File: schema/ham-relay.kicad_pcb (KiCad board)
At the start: 2 copper layers, 140 x 98 mm, 66 parts, among them J1 DB9, P1 JTAG, P2 CONN_01X08, P3 RESET, P4 ISP, P5 CONN_01X03, U1 REG3V3, U2 LPC1114FN28/102, U3 CPC1017N, U4 XYZ, U5 XYZ, U6 TBB1458, U7 74HC126N

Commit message: Design rules
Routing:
- net VCC: track 129.4 -> 0.00 mm
- net /SWDIO: track 48.3 -> 0.00 mm
- net +12V: track 24.8 -> 0.00 mm
- net /RX_CR: track 19.7 -> 0.00 mm
- net /TONE: track 15.5 -> 0.00 mm
- net Net-(P1-Pad17): track 12.1 -> 0.00 mm
- net Net-(P1-Pad11): track 10.8 -> 0.00 mm
- net /TONE_SW: track 8.26 -> 0.00 mm
- net Net-(D1-Pad2): track 7.03 -> 0.00 mm
- net VCC/2: track 6.98 -> 0.00 mm
- net Net-(D4-Pad2): track 6.26 -> 0.00 mm
- net Net-(D6-Pad2): track 6.19 -> 0.00 mm
- net Net-(D3-Pad2): track 6.18 -> 0.00 mm
- net Net-(D5-Pad2): track 6.17 -> 0.00 mm
- net Net-(R10-Pad2): track 5.71 -> 0.00 mm
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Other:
- net class Default: clearance 0.5 -> 0.2032; trace_width 1 -> 0.1524; via_dia 2.5 -> 0.65; via_drill 1 -> 0.3
- net class Small removed
- rule trace_clearance: 0.5 -> 0.2032
- rule trace_min: 0.2 -> 0.15
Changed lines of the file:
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@@
   (general
     (links 151)
-    (no_connects 128)
-    (area 57.709999 38.024999 197.860001 136.175001)
+    (no_connects 151)
+    (area -486.6365 -522.26 736.73 673.46449)
     (thickness 1.6)
     (drawings 8)
-    (tracks 54)
+    (tracks 0)
     (zones 0)
     (modules 66)
@@
   )
   (setup
-    (last_trace_width 1)
-    (trace_clearance 0.5)
+    (last_trace_width 0.1524)
+    (trace_clearance 0.2032)
     (zone_clearance 0.254)
     (zone_45_only yes)
-    (trace_min 0.2)
+    (trace_min 0.15)
     (segment_width 0.2)
     (edge_width 0.15)
-    (via_size 2.5)
-    (via_drill 1)
+    (via_size 0.65)
+    (via_drill 0.3)
     (via_min_size 0.4)
     (via_min_drill 0.3)
@@
   (net 49 "Net-(U2-Pad28)")
   (net_class Default "This is the default net class."
-    (clearance 0.5)
-    (trace_width 1)
-    (via_dia 2.5)
-    (via_drill 1)
+    (clearance 0.2032)
+    (trace_width 0.1524)
+    (via_dia 0.65)
+    (via_drill 0.3)
     (uvia_dia 0.3)
     (uvia_drill 0.1)
@@
     (add_net VCC)
     (add_net VCC/2)
-  )
-  (net_class Small ""
-    (clearance 508)
-    (trace_width 254)
-    (via_dia 2.5)
-    (via_drill 1)
-    (uvia_dia 0.3)
-    (uvia_drill 0.1)
   )
   (module Pin_Headers:Pin_Header_Straight_2x10 (layer F.Cu)
@@
   (gr_line (start 57.785 38.1) (end 197.785 38.1) (angle 90) (layer Edge.Cuts) (width 0.15))
   (gr_line (start 57.785 38.1) (end 57.785 136.1) (angle 90) (layer Edge.Cuts) (width 0.15))
-  (segment (start 80.01 76.835) (end 82.55 76.835) (width 1) (layer B.Cu) (net 2))
-  (segment (start 191.135 50.165) (end 189.865 50.165) (width 1) (layer B.Cu) (net 5))
-  (segment (start 193.04 64.77) (end 194.945 62.865) (width 1) (layer B.Cu) (net 5))
-  (segment (start 194.945 62.865) (end 194.945 53.975) (width 1) (layer B.Cu) (net 5))
-  (segment (start 194.945 53.975) (end 191.135 50.165) (width 1) (layer B.Cu) (net 5))
-  (segment (start 193.04 68.505) (end 193.04 64.77) (width 1) (layer B.Cu) (net 5))
-  (segment (start 189.27064 49.57064) (end 189.27064 47.625) (width 1) (layer B.Cu) (net 5))
-  (segment (start 189.865 50.165) (end 189.27064 49.57064) (width 1) (layer B.Cu) (net 5))
-  (segment (start 185.42 64.135) (end 187.96 64.135) (width 1) (layer B.Cu) (net 6))
-  (segment (start 187.96 64.135) (end 191.135 60.96) (width 1) (layer B.Cu) (net 6))
-  (segment (start 193.04 98.505) (end 188.675 98.505) (width 1) (layer B.Cu) (net 8))
-  (segment (start 188.595 104.14) (end 184.15 104.14) (width 1) (layer B.Cu) (net 8))
-  (segment (start 188.595 98.585) (end 188.595 104.14) (width 1) (layer B.Cu) (net 8))
-  (segment (start 188.675 98.505) (end 188.595 98.585) (width 1) (layer B.Cu) (net 8))
-  (segment (start 179.705 106.045) (end 182.245 106.045) (width 1) (layer B.Cu) (net 8))
-  (segment (start 182.245 106.045) (end 184.15 104.14) (width 1) (layer B.Cu) (net 8))
-  (segment (start 71.755 61.595) (end 66.29 61.595) (width 1) (layer B.Cu) (net 10))
-  (segment (start 66.29 61.595) (end 65.785 62.1) (width 1) (layer B.Cu) (net 10))
-  (segment (start 71.755 48.26) (end 65.945 48.26) (width 1) (layer B.Cu) (net 11))
-  (segment (start 65.945 48.26) (end 65.785 48.1) (width 1) (layer B.Cu) (net 11))
-  (segment (start 65.945 48.26) (end 65.785 48.1) (width 1) (layer F.Cu) (net 11))
-  (segment (start 71.755 54.61) (end 66.275 54.61) (width 1) (layer B.Cu) (net 12))
-  (segment (start 66.275 54.61) (end 65.785 55.1) (width 1) (layer B.Cu) (net 12))
-  (segment (start 151.765 95.885) (end 151.765 87.63) (width 1) (layer B.Cu) (net 15))
-  (segment (start 127 91.44) (end 137.16 91.44) (width 1) (layer B.Cu) (net 16))
-  (segment (start 137.16 91.44) (end 140.97 87.63) (width 1) (layer B.Cu) (net 16))
-  (segment (start 168.275 90.805) (end 172.085 90.805) (width 1) (layer B.Cu) (net 18))
-  (segment (start 173.94936 47.625) (end 173.94936 47.58436) (width 1) (layer B.Cu) (net 19))
-  (segment (start 173.94936 47.58436) (end 173.90872 47.625) (width 1) (layer B.Cu) (net 19))
-  (segment (start 173.90872 47.625) (end 80.01 47.625) (width 1) (layer B.Cu) (net 19))
-  (segment (start 80.01 47.625) (end 79.375 48.26) (width 1) (layer B.Cu) (net 19))
-  (segment (start 171.45 56.515) (end 171.45 55.20436) (width 1) (layer B.Cu) (net 19))
-  (segment (start 171.45 55.20436) (end 173.94936 52.705) (width 1) (layer B.Cu) (net 19))
-  (segment (start 179.705 64.135) (end 179.705 62.23) (width 1) (layer B.Cu) (net 19))
-  (segment (start 179.705 62.23) (end 185.42 56.515) (width 1) (layer B.Cu) (net 19))
-  (segment (start 171.45 56.515) (end 165.735 56.515) (width 1) (layer B.Cu) (net 19))
-  (segment (start 171.45 56.515) (end 174.625 56.515) (width 1) (layer B.Cu) (net 19))
-  (segment (start 174.625 56.515) (end 179.07 56.515) (width 1) (layer B.Cu) (net 19))
-  (segment (start 179.07 56.515) (end 185.42 56.515) (width 1) (layer B.Cu) (net 19))
-  (segment (start 161.925 65.405) (end 165.735 65.405) (width 1) (layer B.Cu) (net 20))
-  (segment (start 165.735 67.31) (end 165.735 65.405) (width 1) (layer B.Cu) (net 20))
-  (segment (start 165.735 65.405) (end 165.735 64.135) (width 1) (layer B.Cu) (net 20))
-  (segment (start 71.755 68.58) (end 66.305 68.58) (width 1) (layer B.Cu) (net 23))
-  (segment (start 66.305 68.58) (end 65.785 69.1) (width 1) (layer B.Cu) (net 23))
-  (segment (start 80.01 84.455) (end 75.565 84.455) (width 1) (layer B.Cu) (net 25))
-  (segment (start 99.06 87.63) (end 99.06 91.44) (width 1) (layer B.Cu) (net 25))
-  (segment (start 85.09 73.66) (end 99.06 87.63) (width 1) (layer B.Cu) (net 25))
-  (segment (start 75.565 73.66) (end 85.09 73.66) (width 1) (layer B.Cu) (net 25))
-  (segment (start 75.565 84.455) (end 75.565 73.66) (width 1) (layer B.Cu) (net 25))
-  (segment (start 151.765 80.01) (end 146.05 80.01) (width 1) (layer B.Cu) (net 36))
-  (segment (start 69.215 89.535) (end 80.01 89.535) (width 1) (layer B.Cu) (net 41))
-  (segment (start 69.215 93.98) (end 73.025 93.98) (width 1) (layer B.Cu) (net 42))
-  (segment (start 76.2 97.155) (end 80.01 97.155) (width 1) (layer B.Cu) (net 42))
-  (segment (start 73.025 93.98) (end 76.2 97.155) (width 1) (layer B.Cu) (net 42))
   (zone (net 0) (net_name "") (layer F.Cu) (hatch edge 0.508)
     (connect_pads (clearance 0))

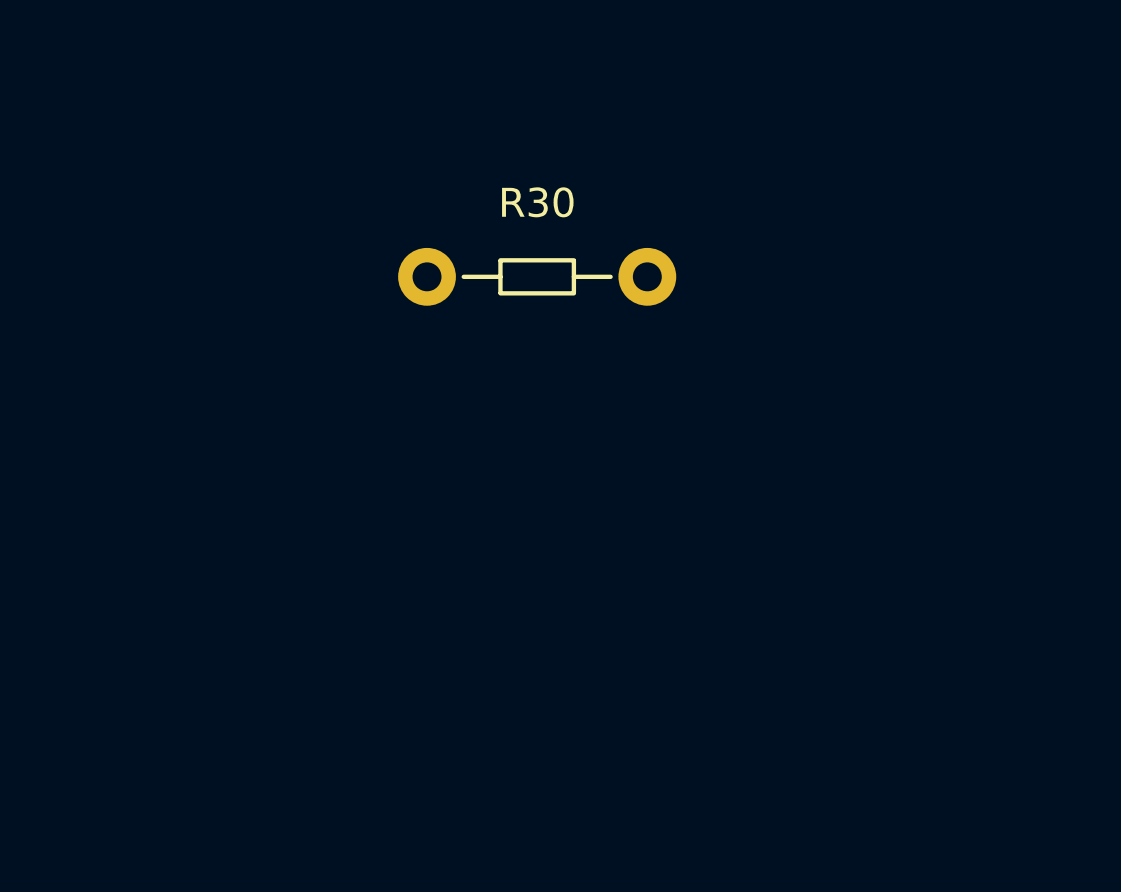
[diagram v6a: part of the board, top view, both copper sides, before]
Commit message: Add EXT_CR support
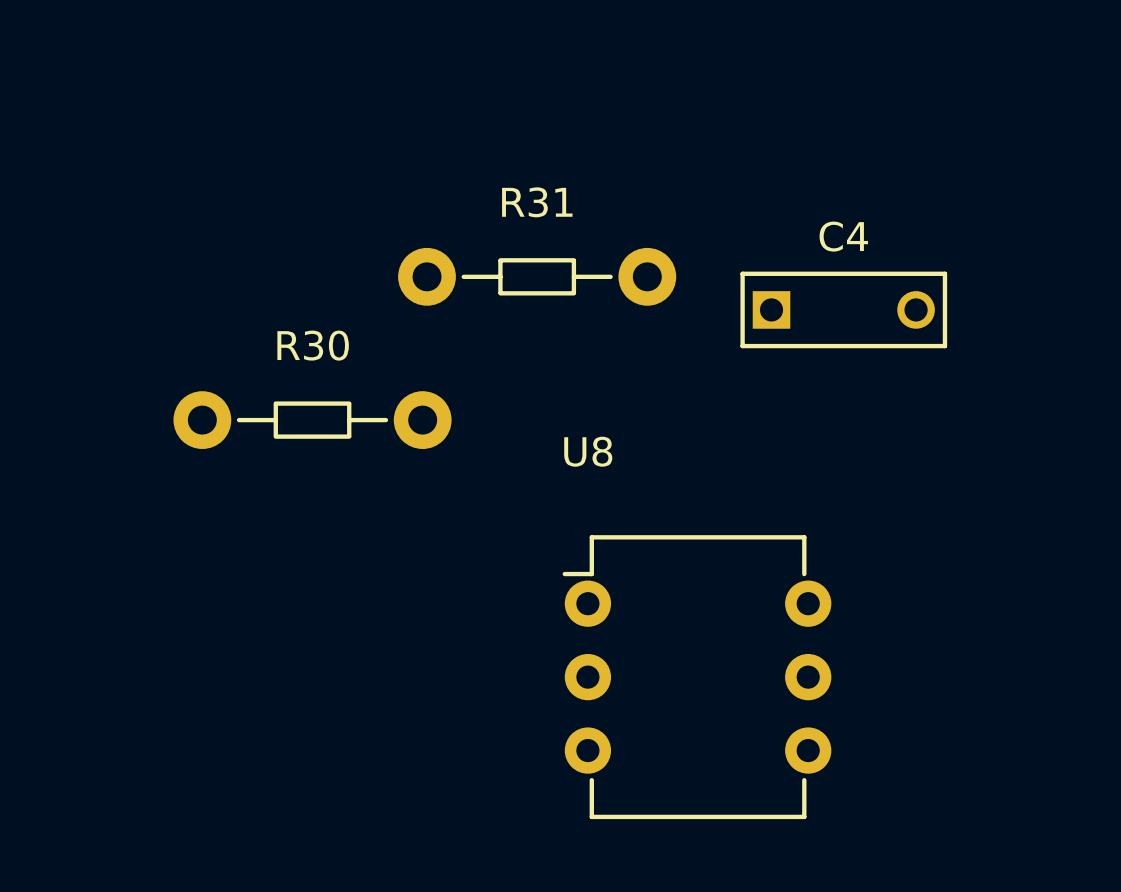
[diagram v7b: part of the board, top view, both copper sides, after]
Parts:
- added C4: 10nF, Capacitors_ThroughHole:C_Rect_L7_W2.5_P5, F.Cu at (135.9, 147.3)
- added R31: ?, resistors:Resistor_Horizontal_RM08mm, F.Cu at (127.8, 146.2)
- added U8: XYZ, Housings_DIP:DIP-6_W7.62mm, F.Cu at (129.5, 157.5)
- moved R30 9.22 mm to (120.0, 151.1)
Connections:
- P2 pad 4: /Audio/AUDIO_IN -> /EXT_CR
- P2 pad 5: /Audio/AUDIO_OUT -> /Audio/AUDIO_IN
- P2 pad 6: (no net) -> /Audio/AUDIO_OUT
- U1 pad 1: VCC -> (no net)
- U1 pad 2: GND -> (no net)
- U1 pad 3: +3V3 -> (no net)
- U2 pad 26: (no net) -> /EXT
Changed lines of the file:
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@@
 (kicad_pcb (version 4) (host pcbnew 4.0.1-stable)
   (general
-    (links 151)
-    (no_connects 151)
-    (area -486.6365 -522.26 736.73 673.46449)
+    (links 155)
+    (no_connects 155)
+    (area 57.709999 38.024999 197.860001 136.175001)
     (thickness 1.6)
     (drawings 8)
     (tracks 0)
     (zones 0)
-    (modules 66)
-    (nets 50)
+    (modules 69)
+    (nets 53)
   )
   (page A4)
@@
   (net 48 "Net-(U2-Pad9)")
   (net 49 "Net-(U2-Pad28)")
+  (net 50 /EXT_CR)
+  (net 51 "Net-(R31-Pad2)")
+  (net 52 /EXT)
   (net_class Default "This is the default net class."
     (clearance 0.2032)
@@
     (add_net /Audio/AUDIO_OUT)
     (add_net /Audio/TONE)
+    (add_net /EXT)
+    (add_net /EXT_CR)
     (add_net /ISP)
     (add_net /RESET)
@@
     (add_net "Net-(R26-Pad2)")
     (add_net "Net-(R30-Pad1)")
+    (add_net "Net-(R31-Pad2)")
     (add_net "Net-(U2-Pad28)")
     (add_net "Net-(U2-Pad5)")
@@
       (net 43 /ISP))
     (pad 25 thru_hole oval (at 15.24 7.62 270) (size 1.6 1.6) (drill 0.8) (layers *.Cu *.Mask F.SilkS))
-    (pad 26 thru_hole oval (at 15.24 5.08 270) (size 1.6 1.6) (drill 0.8) (layers *.Cu *.Mask F.SilkS))
+    (pad 26 thru_hole oval (at 15.24 5.08 270) (size 1.6 1.6) (drill 0.8) (layers *.Cu *.Mask F.SilkS)
+      (net 52 /EXT))
     (pad 27 thru_hole oval (at 15.24 2.54 270) (size 1.6 1.6) (drill 0.8) (layers *.Cu *.Mask F.SilkS)
       (net 14 /RXE))
@@
       (net 5 +12V))
     (pad 7 thru_hole circle (at 30 0 90) (size 2.5 2.5) (drill 1.3) (layers *.Cu *.Mask F.SilkS))
-    (pad 6 thru_hole circle (at 25 0 90) (size 2.5 2.5) (drill 1.3) (layers *.Cu *.Mask F.SilkS))
+    (pad 6 thru_hole circle (at 25 0 90) (size 2.5 2.5) (drill 1.3) (layers *.Cu *.Mask F.SilkS)
+      (net 24 /Audio/AUDIO_OUT))
     (pad 5 thru_hole circle (at 20 0 90) (size 2.5 2.5) (drill 1.3) (layers *.Cu *.Mask F.SilkS)
-      (net 24 /Audio/AUDIO_OUT))
+      (net 28 /Audio/AUDIO_IN))
     (pad 4 thru_hole circle (at 15 0 90) (size 2.5 2.5) (drill 1.3) (layers *.Cu *.Mask F.SilkS)
-      (net 28 /Audio/AUDIO_IN))
+      (net 50 /EXT_CR))
     (pad 3 thru_hole circle (at 10 0 90) (size 2.5 2.5) (drill 1.3) (layers *.Cu *.Mask F.SilkS)
       (net 9 /TX_CR))
@@
     (fp_line (start 0 -3.683) (end -5.334 -3.683) (layer F.SilkS) (width 0.15))
     (fp_line (start 0 -3.683) (end 5.334 -3.683) (layer F.SilkS) (width 0.15))
-    (pad 2 thru_hole oval (at 0 0 270) (size 2.49936 1.50114) (drill 1.00076) (layers *.Cu *.Mask F.SilkS)
-      (net 1 GND))
-    (pad 1 thru_hole oval (at -2.54 0 270) (size 2.49936 1.50114) (drill 1.00076) (layers *.Cu *.Mask F.SilkS)
-      (net 19 VCC))
-    (pad 3 thru_hole oval (at 2.54 0 270) (size 2.49936 1.50114) (drill 1.00076) (layers *.Cu *.Mask F.SilkS)
-      (net 2 +3V3))
+    (pad 2 thru_hole oval (at 0 0 270) (size 2.49936 1.50114) (drill 1.00076) (layers *.Cu *.Mask F.SilkS))
+    (pad 1 thru_hole oval (at -2.54 0 270) (size 2.49936 1.50114) (drill 1.00076) (layers *.Cu *.Mask F.SilkS))
+    (pad 3 thru_hole oval (at 2.54 0 270) (size 2.49936 1.50114) (drill 1.00076) (layers *.Cu *.Mask F.SilkS))
     (model TO_SOT_Packages_THT.3dshapes/TO-220_Neutral123_Horizontal.wrl
       (at (xyz 0 0 0))
@@
   )
   (module resistors:Resistor_Horizontal_RM08mm (layer F.Cu)
-    (at 127.785 146.175001)
+    (at 120.015 151.13)
     (descr "Resistor, Axial,  RM 10mm, 1/3W,")
     (tags "Resistor, Axial, RM 10mm, 1/3W,")
@@
       (net 1 GND))
   )
+  (module Capacitors_ThroughHole:C_Rect_L7_W2.5_P5 (layer F.Cu)
+    (at 135.89 147.32)
+    (descr "Film Capacitor Length 7mm x Width 2.5mm, Pitch 5mm")
+    (tags Capacitor)
+    (fp_text reference C4 (at 2.5 -2.5) (layer F.SilkS)
+      (effects (font (size 1 1) (thickness 0.15)))
+    )
+    (fp_text value 10nF (at 2.5 2.5) (layer F.Fab)
+      (effects (font (size 1 1) (thickness 0.15)))
+    )
+    (fp_line (start -1.25 -1.5) (end 6.25 -1.5) (layer F.CrtYd) (width 0.05))
+    (fp_line (start 6.25 -1.5) (end 6.25 1.5) (layer F.CrtYd) (width 0.05))
+    (fp_line (start 6.25 1.5) (end -1.25 1.5) (layer F.CrtYd) (width 0.05))
+    (fp_line (start -1.25 1.5) (end -1.25 -1.5) (layer F.CrtYd) (width 0.05))
+    (fp_line (start -1 -1.25) (end 6 -1.25) (layer F.SilkS) (width 0.15))
+    (fp_line (start 6 -1.25) (end 6 1.25) (layer F.SilkS) (width 0.15))
+    (fp_line (start 6 1.25) (end -1 1.25) (layer F.SilkS) (width 0.15))
+    (fp_line (start -1 1.25) (end -1 -1.25) (layer F.SilkS) (width 0.15))
+    (pad 1 thru_hole rect (at 0 0) (size 1.3 1.3) (drill 0.8) (layers *.Cu *.Mask F.SilkS)
+      (net 50 /EXT_CR))
+    (pad 2 thru_hole circle (at 5 0) (size 1.3 1.3) (drill 0.8) (layers *.Cu *.Mask F.SilkS)
+      (net 1 GND))
+  )
+  (module resistors:Resistor_Horizontal_RM08mm (layer F.Cu)
+    (at 127.785 146.175001)
+    (descr "Resistor, Axial,  RM 10mm, 1/3W,")
+    (tags "Resistor, Axial, RM 10mm, 1/3W,")
+    (fp_text reference R31 (at 0 -2.54) (layer F.SilkS)
+      (effects (font (size 1 1) (thickness 0.15)))
+    )
+    (fp_text value ? (at 0 2.4765) (layer F.Fab)
+      (effects (font (size 1 1) (thickness 0.15)))
+    )
+    (fp_line (start -1.27 -0.5715) (end 1.27 -0.5715) (layer F.SilkS) (width 0.15))
+    (fp_line (start 1.27 -0.54) (end 1.27 0.54) (layer F.SilkS) (width 0.15))
+    (fp_line (start 1.27 0.5715) (end -1.27 0.5715) (layer F.SilkS) (width 0.15))
+    (fp_line (start -1.27 0.54) (end -1.27 -0.54) (layer F.SilkS) (width 0.15))
+    (fp_line (start -1.27 0) (end -2.54 0) (layer F.SilkS) (width 0.15))
+    (fp_line (start 1.27 0) (end 2.54 0) (layer F.SilkS) (width 0.15))
+    (pad 1 thru_hole circle (at -3.81 0) (size 1.99898 1.99898) (drill 1.00076) (layers *.Cu *.SilkS *.Mask)
+      (net 19 VCC))
+    (pad 2 thru_hole circle (at 3.81 0) (size 1.99898 1.99898) (drill 1.00076) (layers *.Cu *.SilkS *.Mask)
+      (net 51 "Net-(R31-Pad2)"))
+    (model Resistors_ThroughHole.3dshapes/Resistor_Horizontal_RM10mm.wrl
+      (at (xyz 0 0 0))
+      (scale (xyz 0.4 0.4 0.4))
+      (rotate (xyz 0 0 0))
+    )
+  )
+  (module Housings_DIP:DIP-6_W7.62mm (layer F.Cu)
+    (at 129.54 157.48)
+    (descr "6-lead dip package, row spacing 7.62 mm (300 mils)")
+    (tags "dil dip 2.54 300")
+    (fp_text reference U8 (at 0 -5.22) (layer F.SilkS)
+      (effects (font (size 1 1) (thickness 0.15)))
+    )
+    (fp_text value XYZ (at 0 -3.72) (layer F.Fab)
+      (effects (font (size 1 1) (thickness 0.15)))
+    )
+    (fp_line (start -1.05 -2.45) (end -1.05 7.55) (layer F.CrtYd) (width 0.05))
+    (fp_line (start 8.65 -2.45) (end 8.65 7.55) (layer F.CrtYd) (width 0.05))
+    (fp_line (start -1.05 -2.45) (end 8.65 -2.45) (layer F.CrtYd) (width 0.05))
+    (fp_line (start -1.05 7.55) (end 8.65 7.55) (layer F.CrtYd) (width 0.05))
+    (fp_line (start 0.135 -2.295) (end 0.135 -1.025) (layer F.SilkS) (width 0.15))
+    (fp_line (start 7.485 -2.295) (end 7.485 -1.025) (layer F.SilkS) (width 0.15))
+    (fp_line (start 7.485 7.375) (end 7.485 6.105) (layer F.SilkS) (width 0.15))
+    (fp_line (start 0.135 7.375) (end 0.135 6.105) (layer F.SilkS) (width 0.15))
+    (fp_line (start 0.135 -2.295) (end 7.485 -2.295) (layer F.SilkS) (width 0.15))
+    (fp_line (start 0.135 7.375) (end 7.485 7.375) (layer F.SilkS) (width 0.15))
+    (fp_line (start 0.135 -1.025) (end -0.8 -1.025) (layer F.SilkS) (width 0.15))
+    (pad 1 thru_hole oval (at 0 0) (size 1.6 1.6) (drill 0.8) (layers *.Cu *.Mask F.SilkS)
+      (net 51 "Net-(R31-Pad2)"))
+    (pad 2 thru_hole oval (at 0 2.54) (size 1.6 1.6) (drill 0.8) (layers *.Cu *.Mask F.SilkS)
+      (net 50 /EXT_CR))
+    (pad 3 thru_hole oval (at 0 5.08) (size 1.6 1.6) (drill 0.8) (layers *.Cu *.Mask F.SilkS))
+    (pad 4 thru_hole oval (at 7.62 5.08) (size 1.6 1.6) (drill 0.8) (layers *.Cu *.Mask F.SilkS)
+      (net 1 GND))
+    (pad 5 thru_hole oval (at 7.62 2.54) (size 1.6 1.6) (drill 0.8) (layers *.Cu *.Mask F.SilkS)
+      (net 52 /EXT))
+    (pad 6 thru_hole oval (at 7.62 0) (size 1.6 1.6) (drill 0.8) (layers *.Cu *.Mask F.SilkS))
+    (model Housings_DIP.3dshapes/DIP-6_W7.62mm.wrl
+      (at (xyz 0 0 0))
+      (scale (xyz 1 1 1))
+      (rotate (xyz 0 0 0))
+    )
+  )
   (gr_circle (center 183.285 41.1) (end 185.035 41.1) (layer Edge.Cuts) (width 0.15))

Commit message: Component placement
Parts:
- moved C15 101.1 mm to (149.9, 57.1), turned to 0 degrees
- moved R2 97.8 mm to (102.2, 85.7), turned to 180 degrees
- moved C10 82.6 mm to (105.4, 73.7), turned to 270 degrees
- moved R24 81.9 mm to (95.2, 73.0), turned to 180 degrees
- moved C13 79.8 mm to (125.7, 76.8)
- moved C4 79.2 mm to (164.5, 67.9), turned to 90 degrees
- moved RV2 77.7 mm to (142.2, 87.6)
- moved RV1 76.7 mm to (117.5, 87.6)
- moved C14 76.2 mm to (135.3, 76.8)
- moved R25 74.1 mm to (118.7, 73.0)
- moved R27 72.3 mm to (118.7, 61.0)
- moved R26 71.3 mm to (143.5, 73.0)
- moved R21 71.3 mm to (95.2, 68.6), turned to 0 degrees
- moved R20 70.4 mm to (105.4, 64.8), turned to 90 degrees
- moved R28 69.5 mm to (143.5, 61.0)
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- renumbered C5 to C4, C6 to C5, C7 to C6, C4 to C7, D3 to D2, D2 to D3, R8 to R10, R31 to R12, R12 to R13, R13 to R14, R14 to R15, R15 to R16, R16 to R17, R17 to R18, R18 to R19, R19 to R20, R20 to R21, R21 to R22, R22 to R23, R30 to R24, R23 to R25, R24 to R26, R25 to R27, R26 to R28, R27 to R29, R28 to R30, R29 to R31, R9 to R8, R10 to R9, U3 to U2, U2 to U3, U8 to U4, U4 to U5, U7 to U6, U5 to U7, U6 to U8
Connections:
- U1 pad 1: (no net) -> VCC
- U1 pad 2: (no net) -> GND
- U1 pad 3: (no net) -> +3V3
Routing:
- removed copper zone on B.Cu, net +12V
- removed copper zone on B.Cu, net VCC
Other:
- net class Default: trace_width 0.1524 -> 0.508; via_dia 0.65 -> 1.5; via_drill 0.3 -> 0.5
